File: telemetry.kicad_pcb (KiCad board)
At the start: 2 copper layers, 152 x 79.5 mm, 70 parts, among them J1 Conn_01x03, J10 DT13-2P, J11 Conn_01x03, J12 Conn_01x03, J13 Conn_01x03, J14 Conn_01x06, J15 Conn_01x03, J16 Conn_01x03, J17 Conn_01x03, J18 Conn_01x03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

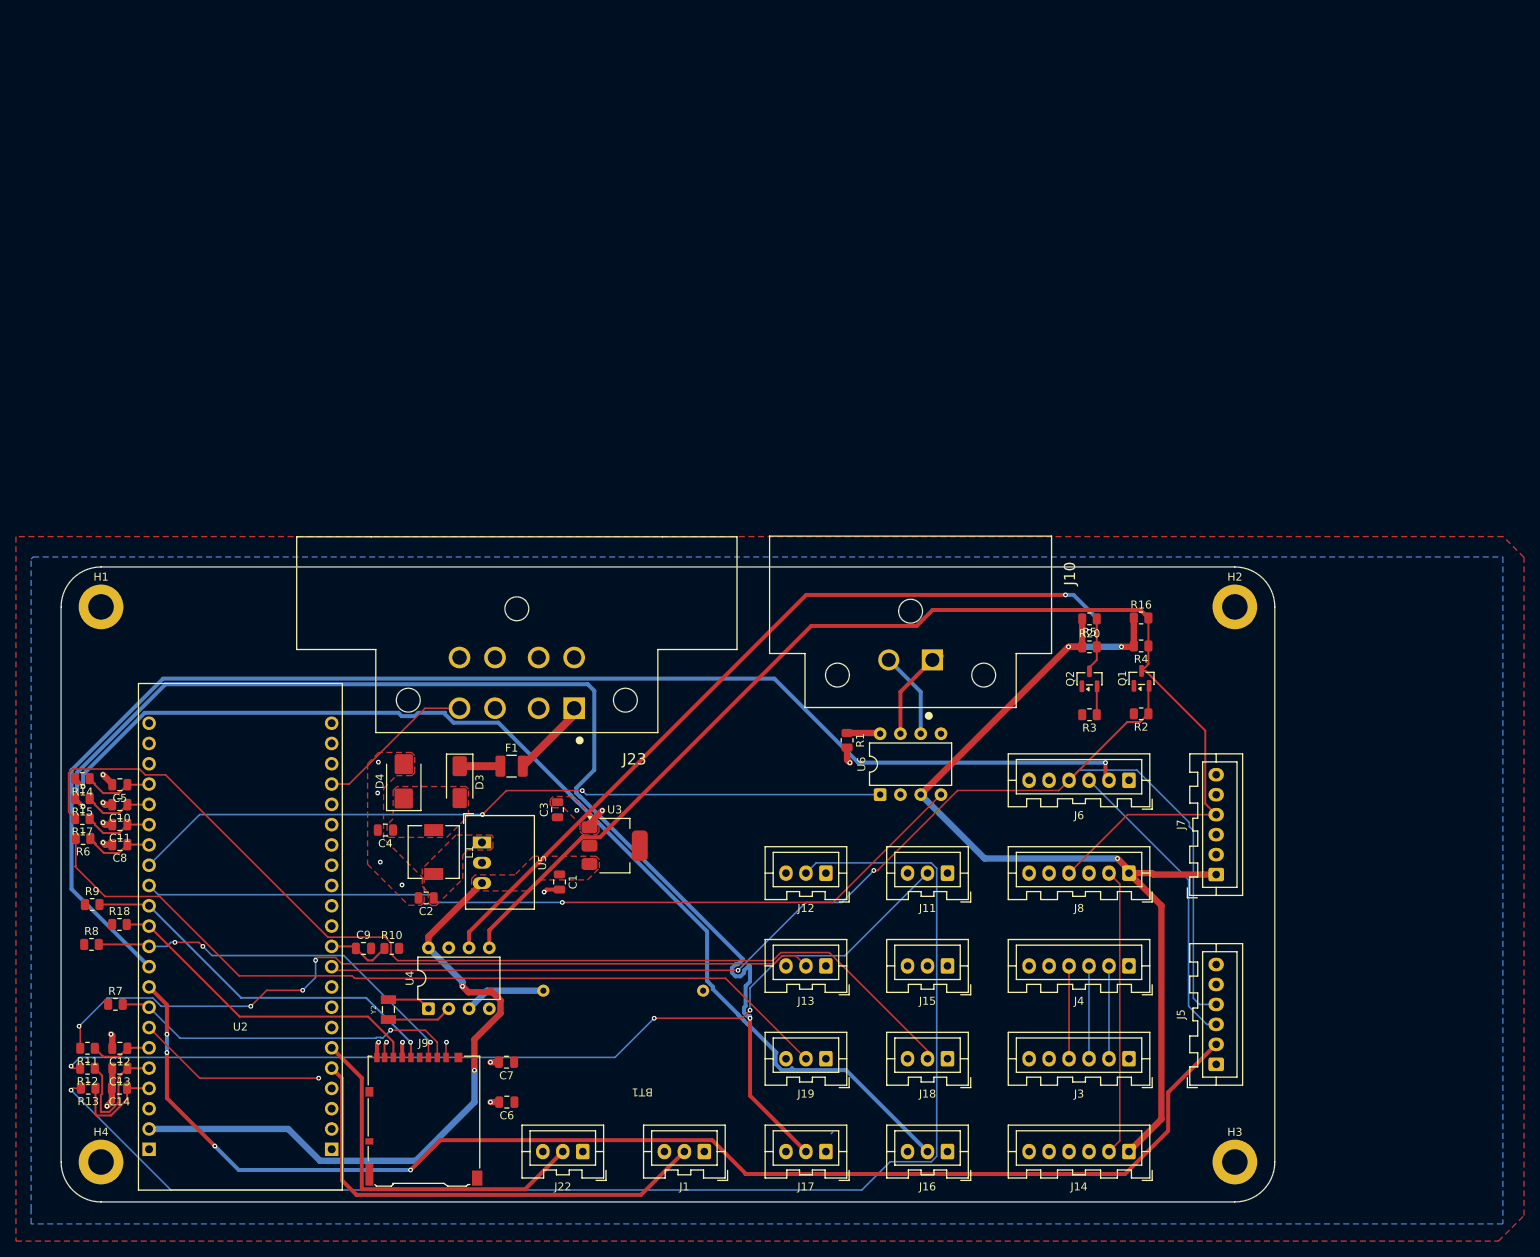
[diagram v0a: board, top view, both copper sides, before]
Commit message: Move ESP32 to center
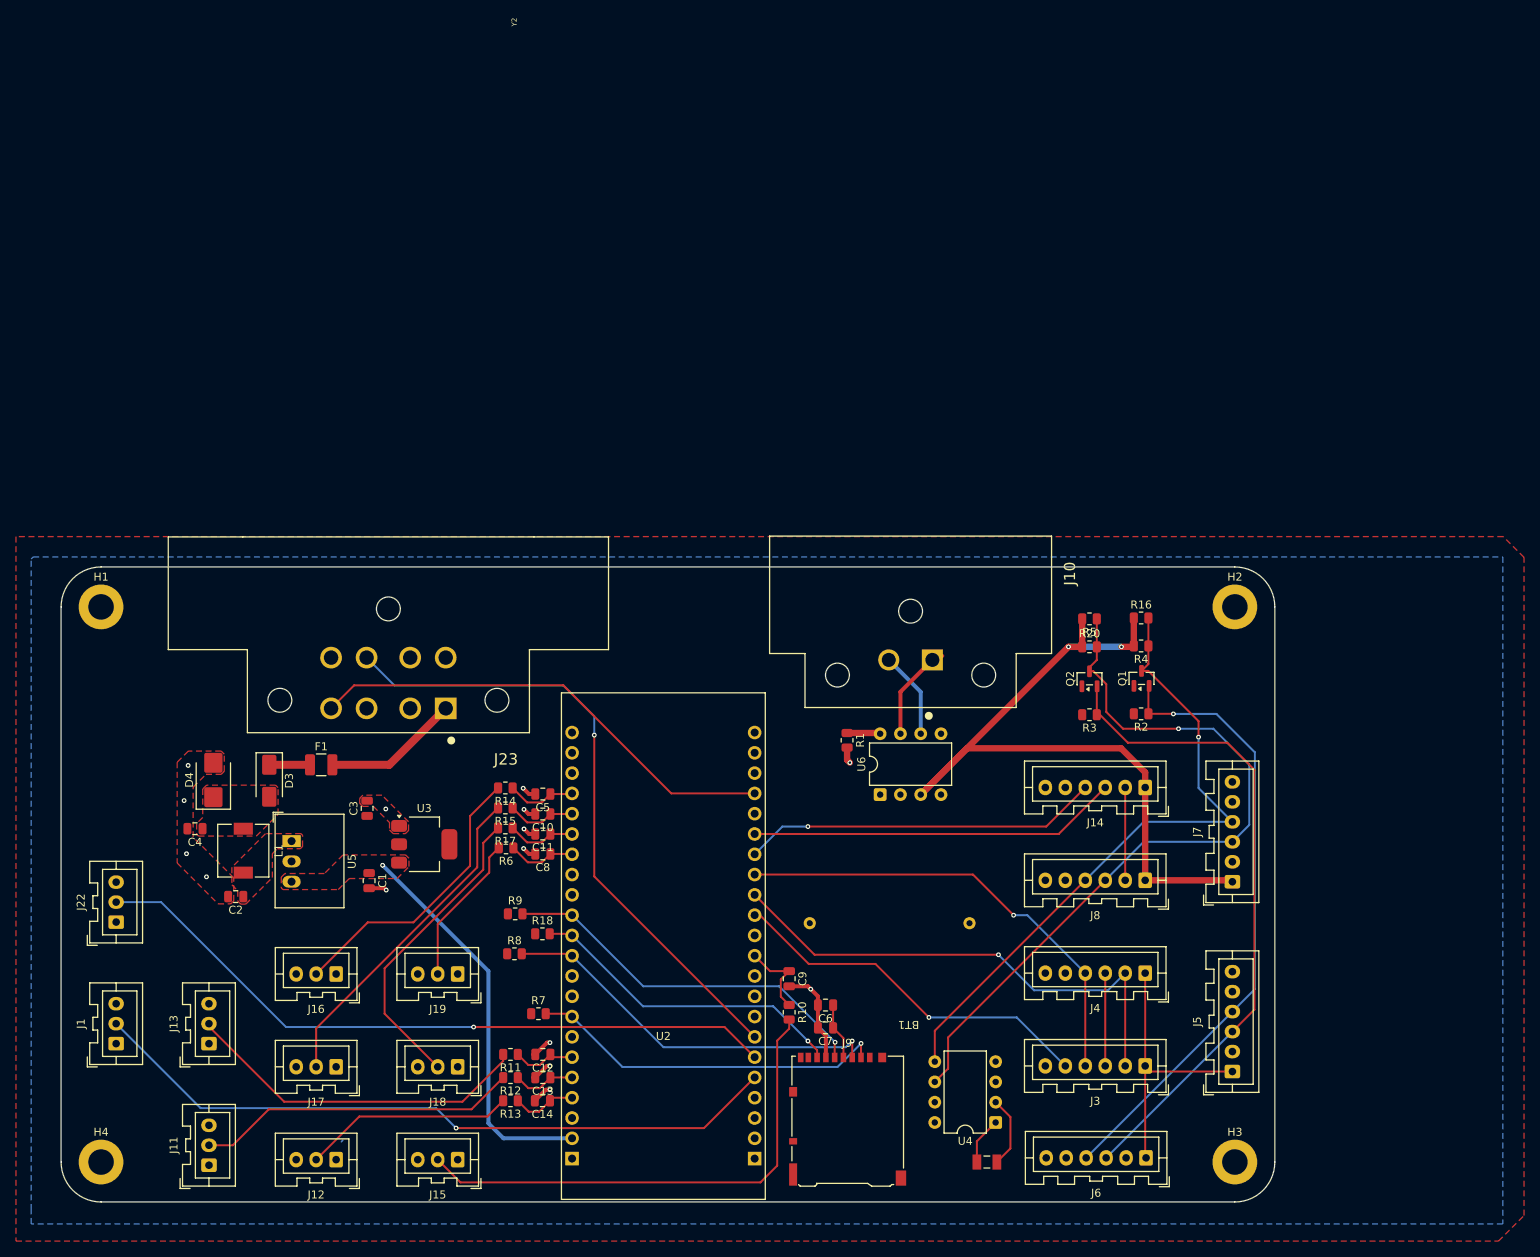
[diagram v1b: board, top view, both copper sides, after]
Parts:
- moved J11 99.4 mm to (63.8, 134.9), turned to 90 degrees
- moved J16 79.7 mm to (79.7, 111.0)
- moved J13 77.9 mm to (63.8, 119.7), turned to 90 degrees
- moved Y2 77.3 mm to (161.2, 134.5), turned to 180 degrees
- moved J1 74.9 mm to (52.1, 119.7), turned to 90 degrees
- moved U4 72.4 mm to (162.2, 129.6), turned to 180 degrees
- moved J12 71.0 mm to (79.7, 134.2)
- moved J15 65.9 mm to (94.9, 134.2)
- moved J22 65.1 mm to (52.1, 104.5), turned to 90 degrees
- moved J17 62.2 mm to (79.7, 122.6)
- moved J18 61.3 mm to (94.9, 122.6)
- moved C9 53.4 mm to (136.4, 111.5), turned to -90 degrees
- moved J9 53.0 mm to (143.7, 129.1)
- moved C14 53.0 mm to (105.5, 126.8)
- moved U2 53.0 mm to (120.7, 118.2)
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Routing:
- net /I2C0_1_GPIO: track 169.6 -> 0.00 mm, vias 1 -> 0
- net /I2C0_0_GPIO: track 162.9 -> 0.00 mm, vias 4 -> 0
- net /A7_SIG: track 169.9 -> 26.5 mm, vias 1 -> 0
- net /A1_SIG: track 151.4 -> 41.8 mm, vias 2 -> 0
- net /CAN_RX: track 105.6 -> 0.00 mm, vias 1 -> 0
- net /A0_SIG: track 140.1 -> 36.1 mm, vias 1 -> 0
- net /CAN_TX: track 95.6 -> 0.00 mm, vias 2 -> 0
- net /A2_SIG: track 131.0 -> 38.5 mm
- net /A3_SIG: track 105.0 -> 19.0 mm
- net /I2C0_SDA: track 163.0 -> 78.3 mm, vias 2 -> 1
- net /W3: track 0.00 -> 80.0 mm, vias 0 -> 1
- net /A6_SIG: track 120.1 -> 40.3 mm, vias 3 -> 0
- net /I2C1_SDA: track 152.3 -> 83.5 mm, vias 0 -> 1
- net /A4_SIG: track 0.00 -> 63.5 mm
- net +5V: track 205.5 -> 148.2 mm, vias 5 -> 3
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
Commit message: Update telemetry.kicad_pcb
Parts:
- moved BT1 22.8 mm to (161.8, 104.6), turned to 0 degrees
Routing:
- net +5V: track 148.2 -> 254.0 mm
- net /I2C0_0_GPIO: track 0.00 -> 104.9 mm, vias 0 -> 3
- net /I2C1_0_GPIO: track 0.00 -> 90.5 mm
- net /I2C0_1_GPIO: track 0.00 -> 80.3 mm, vias 0 -> 3
- net /SPI1_1_CS: track 0.00 -> 74.5 mm, vias 0 -> 1
- net /I2C1_1_GPIO: track 11.6 -> 73.9 mm, vias 0 -> 1
- net /CAN_RX: track 0.00 -> 55.8 mm, vias 0 -> 1
- net /I2C0_SDA: track 78.3 -> 130.9 mm, vias 1 -> 2
- net /SPI1_MOSI: track 11.6 -> 60.7 mm
- net /I2C0_SCL: track 82.4 -> 131.4 mm, vias 0 -> 1
- net /CAN_TX: track 0.00 -> 42.7 mm
- net Net-(BT1-+): track 0.00 -> 29.8 mm
- net GND: track 31.5 -> 51.7 mm, vias 15 -> 16
- net /I2C1_SDA: track 83.5 -> 85.9 mm

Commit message: Fix DRC errors
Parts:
- moved J6 0.16 mm to (181.0, 134.1)
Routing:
- net GND: track 51.7 -> 93.2 mm, vias 16 -> 20
- net +3V3: track 41.5 -> 50.1 mm, vias 0 -> 4
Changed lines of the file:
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@@
 	(footprint "Connector_JST:JST_XA_B06B-XASK-1_1x06_P2.50mm_Vertical"
 		(layer "F.Cu")
-		(at 181.08 133.98 180)
+		(at 180.97 134.09 180)
 		(descr "JST XA series connector, B06B-XASK-1 (https://www.jst.com/wp-content/uploads/2021/01/eXA1.pdf), generated with kicad-footprint-generator")
 		(tags "connector JST XA vertical")
@@
 		)
 	)
-	(gr_arc
-		(start 45.25 65)
-		(mid 46.714466 61.464466)
-		(end 50.25 60)
-		(stroke
-			(width 0.1)
-			(type solid)
-		)
-		(locked yes)
-		(layer "Edge.Cuts")
-	)
 	(gr_line
 		(start 45.25 134.5)
@@
 	)
 	(gr_line
-		(start 50.25 60)
-		(end 192.2 60)
+		(start 50.25 139.5)
+		(end 192.2 139.5)
 		(stroke
 			(width 0.1)
@@
 	)
 	(gr_arc
-		(start 50.25 139.5)
-		(mid 46.714466 138.035534)
-		(end 45.25 134.5)
+		(start 192.200001 60)
+		(mid 195.735535 61.464466)
+		(end 197.200001 65)
 		(stroke
 			(width 0.1)
@@
 		(layer "Edge.Cuts")
 	)
-	(gr_line
-		(start 50.25 139.5)
+	(gr_arc
+		(start 197.2 134.5)
+		(mid 195.735534 138.035534)
 		(end 192.2 139.5)
 		(stroke
@@
 	)
 	(gr_arc
-		(start 192.200001 60)
-		(mid 195.735535 61.464466)
-		(end 197.200001 65)
+		(start 45.25 65)
+		(mid 46.714466 61.464466)
+		(end 50.25 60)
 		(stroke
 			(width 0.1)
@@
 	)
 	(gr_arc
-		(start 197.2 134.5)
-		(mid 195.735534 138.035534)
-		(end 192.2 139.5)
+		(start 50.25 139.5)
+		(mid 46.714466 138.035534)
+		(end 45.25 134.5)
 		(stroke
 			(width 0.1)
@@
 		(layer "Edge.Cuts")
 	)
-	(gr_arc
-		(start 45.25 65)
-		(mid 46.714466 61.464466)
-		(end 50.25 60)
+	(gr_line
+		(start 50.25 60)
+		(end 192.2 60)
 		(stroke
 			(width 0.1)
-			(type default)
+			(type solid)
 		)
 		(locked yes)
-		(layer "Margin")
+		(layer "Edge.Cuts")
 	)
-	(gr_line
-		(start 45.25 134.5)
-		(end 45.25 65)
+	(gr_arc
+		(start 192.200001 60)
+		(mid 195.735535 61.464466)
+		(end 197.200001 65)
 		(stroke
 			(width 0.1)
@@
 		(layer "Margin")
 	)
-	(gr_line
-		(start 50.25 60)
-		(end 192.200001 60)
+	(gr_arc
+		(start 50.25 139.5)
+		(mid 46.714466 138.035534)
+		(end 45.25 134.5)
 		(stroke
 			(width 0.1)
@@
 		(layer "Margin")
 	)
-	(gr_arc
+	(gr_line
 		(start 50.25 139.5)
-		(mid 46.714466 138.035534)
-		(end 45.25 134.5)
+		(end 192.2 139.5)
 		(stroke
 			(width 0.1)
@@
 	)
 	(gr_line
-		(start 50.25 139.5)
-		(end 192.2 139.5)
+		(start 45.25 134.5)
+		(end 45.25 65)
 		(stroke
 			(width 0.1)
@@
 	)
 	(gr_arc
-		(start 192.200001 60)
-		(mid 195.735535 61.464466)
-		(end 197.200001 65)
+		(start 197.2 134.5)
+		(mid 195.735534 138.035534)
+		(end 192.2 139.5)
 		(stroke
 			(width 0.1)
@@
 		(layer "Margin")
 	)
+	(gr_line
+		(start 50.25 60)
+		(end 192.200001 60)
+		(stroke
+			(width 0.1)
+			(type default)
+		)
+		(locked yes)
+		(layer "Margin")
+	)
 	(gr_arc
-		(start 197.2 134.5)
-		(mid 195.735534 138.035534)
-		(end 192.2 139.5)
+		(start 45.25 65)
+		(mid 46.714466 61.464466)
+		(end 50.25 60)
 		(stroke
 			(width 0.1)
@@
 	)
 	(segment
+		(start 168.58 122.58)
+		(end 168.47 122.47)
+		(width 0.5)
+		(layer "F.Cu")
+		(net 2)
+	)
+	(segment
 		(start 140.995 118.695)
 		(end 140 117.7)
@@
 	)
 	(segment
+		(start 186.52 105.3)
+		(end 191.89 110.67)
+		(width 0.5)
+		(layer "F.Cu")
+		(net 2)
+	)
+	(segment
 		(start 140.995 121.41)
 		(end 140.995 118.695)
@@
 	)
 	(segment
+		(start 168.47 134.09)
+		(end 168.47 122.47)
+		(width 0.5)
+		(layer "F.Cu")
+		(net 2)
+	)
+	(segment
+		(start 180.2 105.3)
+		(end 186.52 105.3)
+		(width 0.5)
+		(layer "F.Cu")
+		(net 2)
+	)
+	(segment
 		(start 143.65 82.6125)
 		(end 143.65 84.15)
@@
 	)
 	(segment
+		(start 191.89 89.41)
+		(end 186.11 89.41)
+		(width 0.5)
+		(layer "F.Cu")
+		(net 2)
+	)
+	(segment
 		(start 104.61 93.43)
 		(end 103.83 93.43)
@@
 	)
 	(segment
+		(start 139.1 112.85)
+		(end 139.1 111.15)
+		(width 0.5)
+		(layer "F.Cu")
+		(net 2)
+	)
+	(segment
 		(start 103.83 88.43)
 		(end 103.1 87.7)
@@
 	)
 	(segment
+		(start 139.1 111.15)
+		(end 140.7 109.55)
+		(width 0.5)
+		(layer "F.Cu")
+		(net 2)
+	)
+	(segment
+		(start 168.47 122.47)
+		(end 168.47 119.53)
+		(width 0.5)
+		(layer "F.Cu")
+		(net 2)
+	)
+	(segment
 		(start 104.61 95.93)
 		(end 103.83 95.93)
@@
 	)
 	(segment
+		(start 168.47 119.53)
+		(end 169.2 118.8)
+		(width 0.5)
+		(layer "F.Cu")
+		(net 2)
+	)
+	(segment
 		(start 140.995 122.21)
 		(end 140.995 121.41)
@@
 	)
 	(segment
+		(start 186.11 89.41)
+		(end 184.65 87.95)
+		(width 0.5)
+		(layer "F.Cu")
+		(net 2)
+	)
+	(segment
 		(start 137.345 129.951422)
 		(end 136.046422 131.25)
@@
 	)
 	(via
+		(at 140.7 109.55)
+		(size 0.6)
+		(drill 0.3)
+		(layers "F.Cu" "B.Cu")
+		(net 2)
+	)
+	(via
 		(at 103.2 90.35)
 		(size 0.6)
@@
 	)
 	(via
+		(at 184.65 87.95)
+		(size 0.6)
+		(drill 0.3)
+		(layers "F.Cu" "B.Cu")
+		(net 2)
+	)
+	(via
+		(at 169.2 118.8)
+		(size 0.6)
+		(drill 0.3)
+		(layers "F.Cu" "B.Cu")
+		(net 2)
+	)
+	(via
 		(at 61.15 84.85)
 		(size 0.6)
@@
 	)
 	(via
+		(at 180.2 105.3)
+		(size 0.6)
+		(drill 0.3)
+		(layers "F.Cu" "B.Cu")
+		(net 2)
+	)
+	(via
 		(at 106.45 122.5)
 		(size 0.6)
@@
 		(net 5)
 	)
+	(via
+		(at 189.15 128.1)
+		(size 0.6)
+		(drill 0.3)
+		(layers "F.Cu" "B.Cu")
+		(free yes)
+		(net 5)
+	)
+	(via
+		(at 165.75 72.15)
+		(size 0.6)
+		(drill 0.3)
+		(layers "F.Cu" "B.Cu")
+		(free yes)
+		(net 5)
+	)
+	(via
+		(at 168.9 75.25)
+		(size 0.6)
+		(drill 0.3)
+		(layers "F.Cu" "B.Cu")
+		(free yes)
+		(net 5)
+	)
+	(via
+		(at 192.9 129.1)
+		(size 0.6)
+		(drill 0.3)
+		(layers "F.Cu" "B.Cu")
+		(free yes)
+		(net 5)
+	)
+	(segment
+		(start 191.9 128.1)
+		(end 192.9 129.1)
+		(width 0.5)
+		(layer "B.Cu")
+		(net 5)
+	)
+	(segment
+		(start 165.8 72.15)
+		(end 168.9 75.25)
+		(width 0.5)
+		(layer "B.Cu")
+		(net 5)
+	)
+	(segment
+		(start 189.15 128.1)
+		(end 191.9 128.1)
+		(width 0.5)
+		(layer "B.Cu")
+		(net 5)
+	)
+	(segment
+		(start 165.75 72.15)
+		(end 165.8 72.15)
+		(width 0.25)
+		(layer "B.Cu")
+		(net 5)
+	)
 	(segment
 		(start 103.591 89.481)
@@
 	)
 	(segment
-		(start 138.85 109.7)
-		(end 147.2 109.7)
+		(start 132.74 103.59)
+		(end 137.85 108.7)
 		(width 0.25)
 		(layer "F.Cu")
@@
 	)
 	(segment
-		(start 132.08 103.59)
-		(end 132.74 103.59)
+		(start 137.85 108.7)
+		(end 146.2 108.7)
 		(width 0.25)
 		(layer "F.Cu")
@@
 	)
 	(segment
-		(start 147.2 109.7)
+		(start 146.2 108.7)
 		(end 153.9 116.4)
 		(width 0.25)
@@
 	)
 	(segment
-		(start 132.74 103.59)
-		(end 138.85 109.7)
+		(start 132.08 103.59)
+		(end 132.74 103.59)
 		(width 0.25)
 		(layer "F.Cu")
@@
 	)
 	(segment
+		(start 161.8 107.75)
+		(end 162.6 108.55)
+		(width 0.25)
+		(layer "F.Cu")
+		(net 14)
+	)
+	(segment
 		(start 132.08 101.05)
-		(end 139.58 108.55)
+		(end 138.78 107.75)
 		(width 0.25)
 		(layer "F.Cu")
@@
 	)
 	(segment
-		(start 139.58 108.55)
-		(end 162.6 108.55)
+		(start 138.78 107.75)
+		(end 161.8 107.75)
 		(width 0.25)
 		(layer "F.Cu")

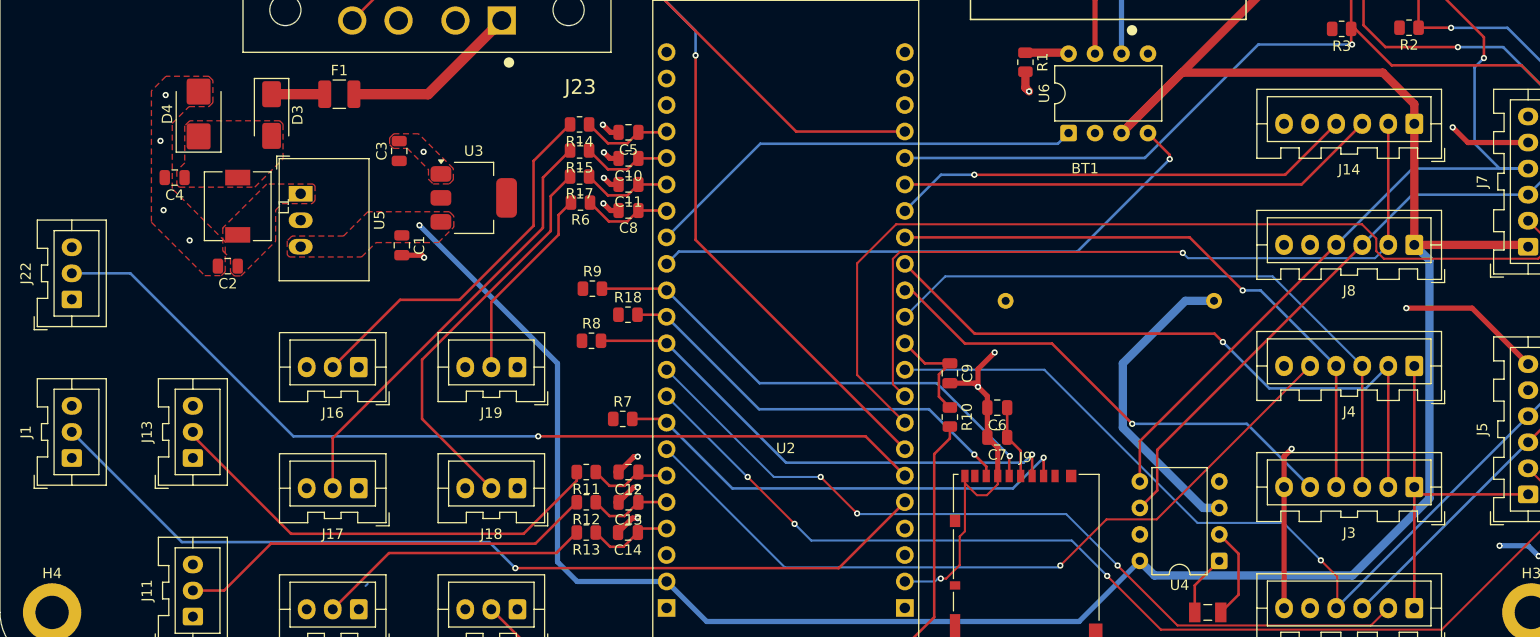
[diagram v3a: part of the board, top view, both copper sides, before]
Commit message: Add text and labels
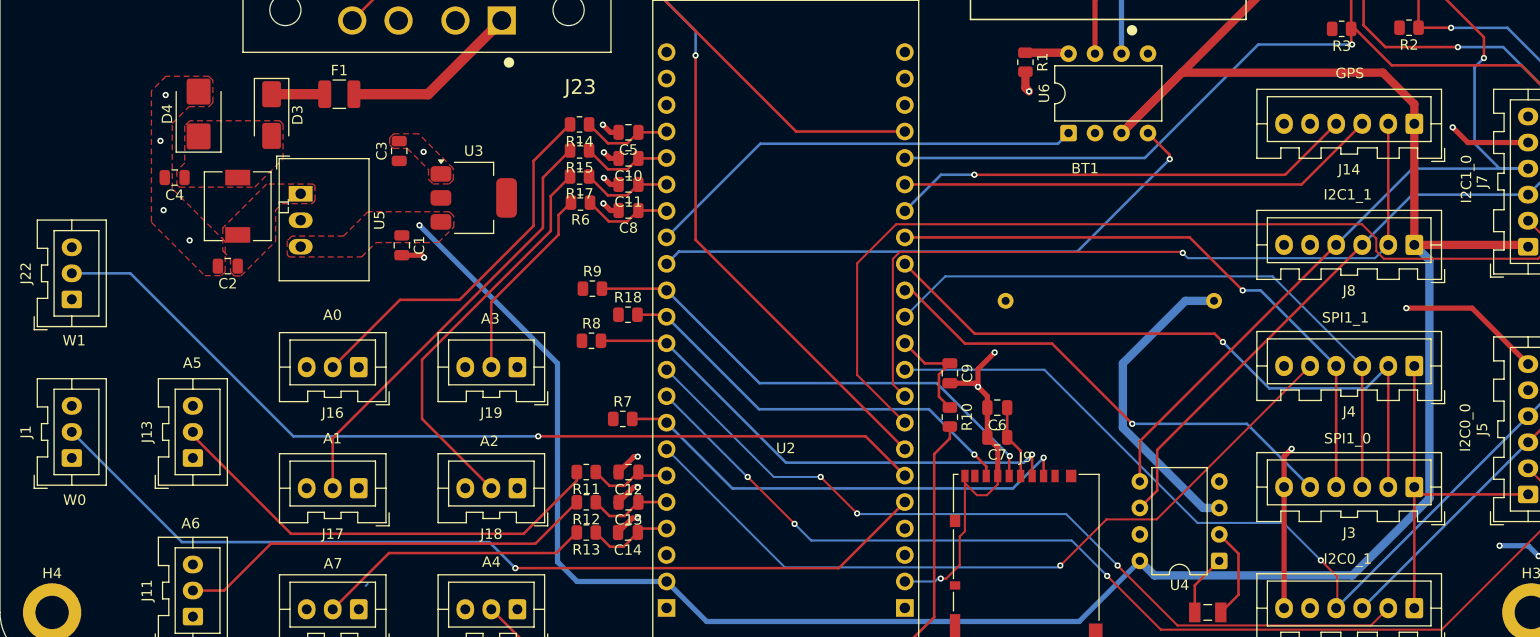
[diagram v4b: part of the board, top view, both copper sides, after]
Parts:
- added Telemetry (2026): LOGO, Telemetry:FBR_Logo_.9in, B.Cu at (58.1, 78.9)
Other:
- board text added: "A0"
- board text added: "A1"
- board text added: "A2"
- board text added: "A3"
- board text added: "A4"
- board text added: "A5"
- board text added: "A6"
- board text added: "A7"
- board text added: "GPS"
- board text added: "I2C0_0"
- board text added: "I2C0_1"
- board text added: "I2C1_0"
- board text added: "I2C1_1"
- board text added: "SPI1_0"
- board text added: "SPI1_1"
- board text added: "W0"
- board text added: "W1"
